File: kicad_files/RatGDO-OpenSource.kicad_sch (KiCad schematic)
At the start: 10 parts, among them J1 Screw_Terminal_01x03, J2 Screw_Terminal_01x03, Q1 2N7002, Q2 AO3400A, U1 WeMos_D1_mini, U2 AMS1117-3.3

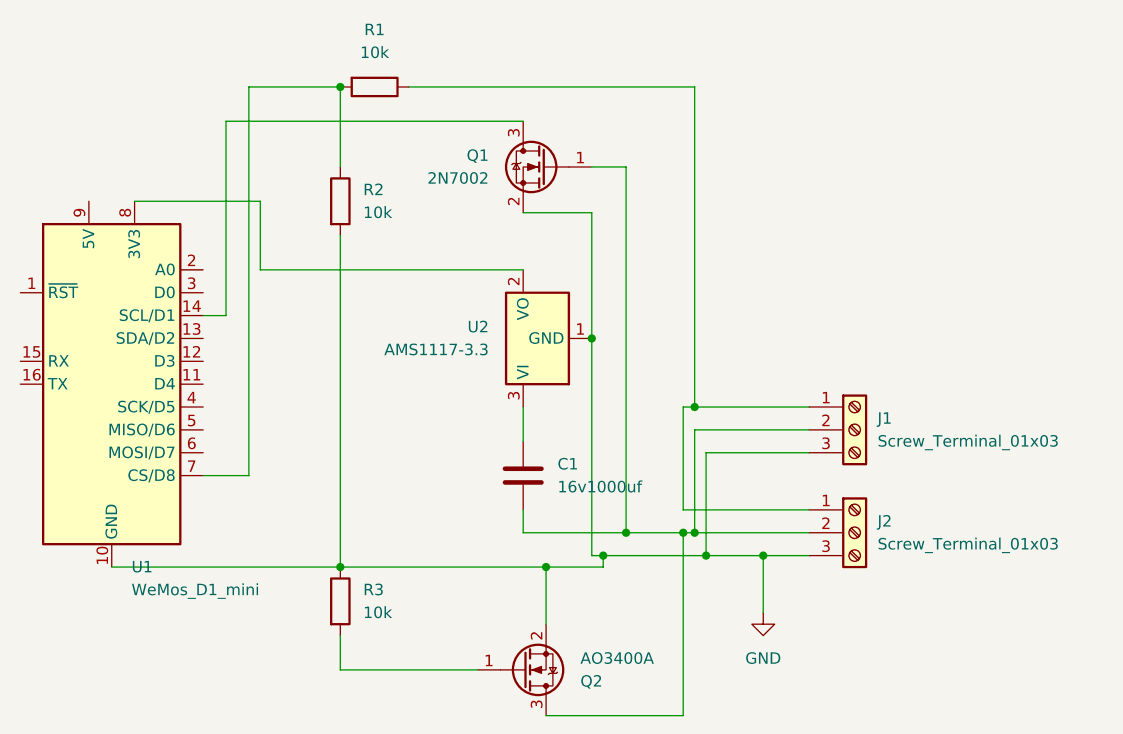
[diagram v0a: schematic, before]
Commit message: Updated Files to match new Schematics
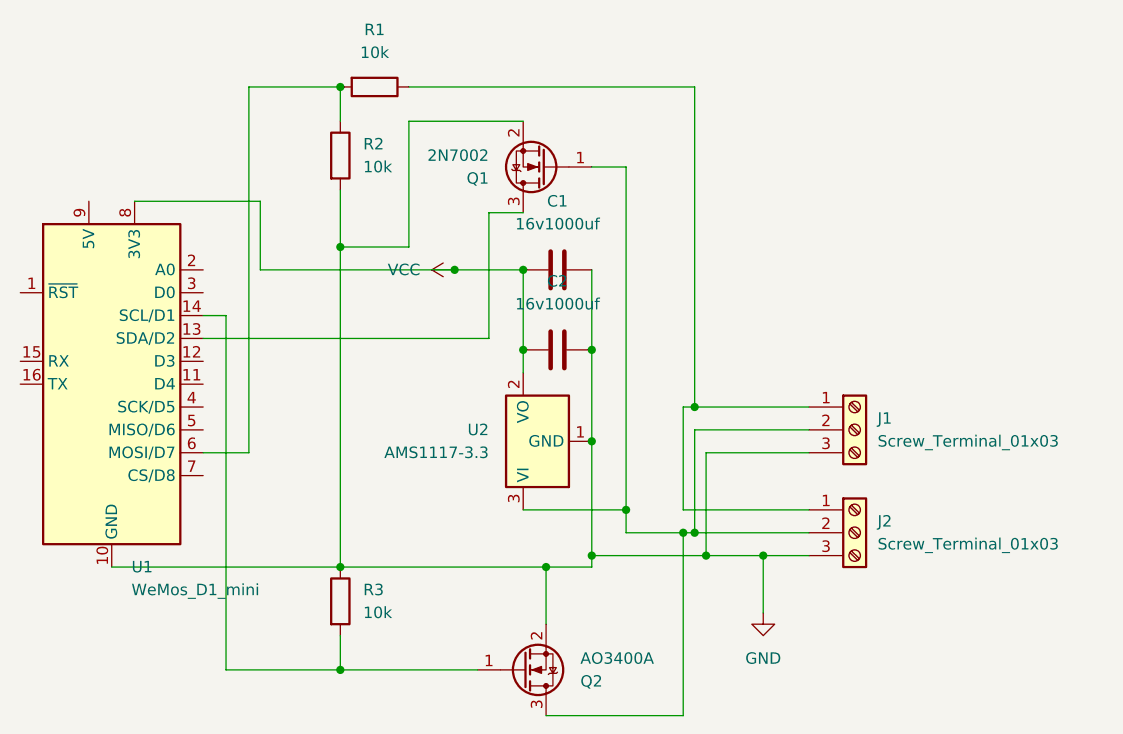
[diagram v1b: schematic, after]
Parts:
- added C2: 16v1000uf, Capacitor_THT:CP_Radial_D10.0mm_P5.00mm, symbol Device:C
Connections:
- net GND: now also C1.2, C2.2
- net at Q2.1 (G), R3.2: now also U1.14 (SCL/D1)
- net at U1.13 (SDA/D2): now also Q1.3 (D)
- net at U1.6 (MOSI/D7): now also R1.2, R2.1
- net VCC: now reaches U1.8 (3V3), U2.2 (VO)
- net VCC: now also C1.1, C2.1
- net at U2.3 (VI): now also J1.2 (Pin_2), J2.2 (Pin_2), Q1.1 (G), Q2.3 (D); no longer C1.1
- now unconnected: U1.7 (CS/D8)
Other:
- moved on the sheet: C1, Q1, R2, U2

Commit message: Remove power supply components
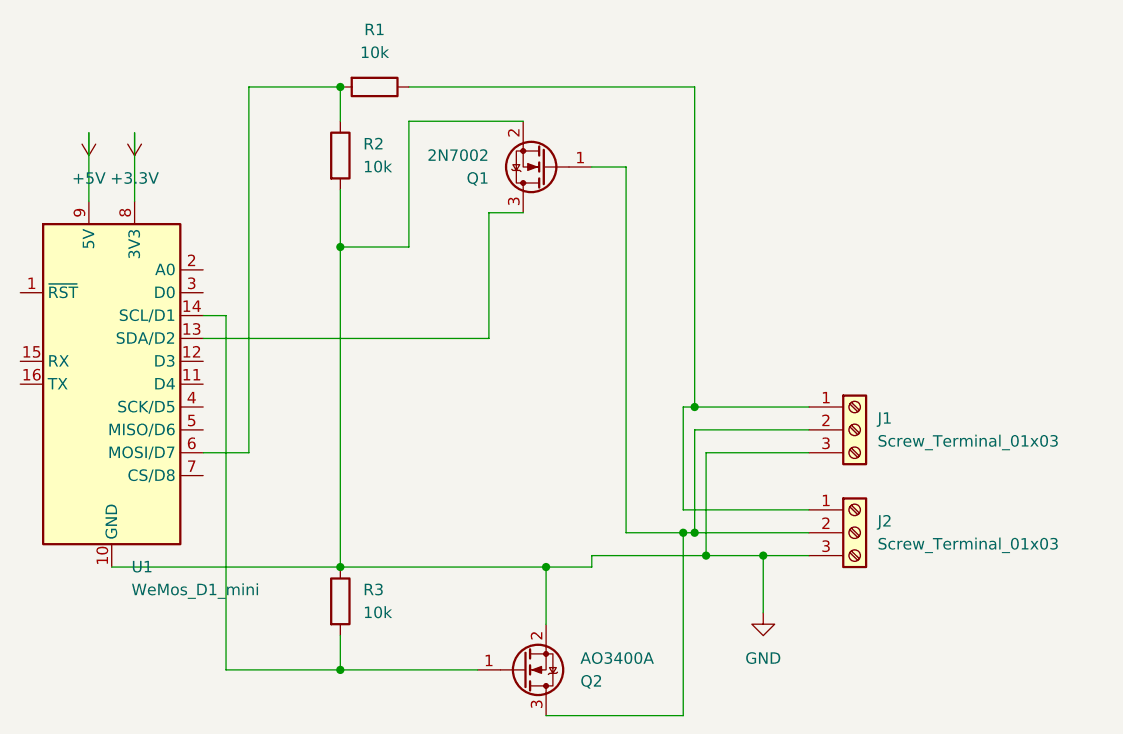
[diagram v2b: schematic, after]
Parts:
- removed C1: 16v1000uf, Capacitor_SMD:CP_Elec_10x10.5, symbol Device:C
- removed C2: 16v1000uf, Capacitor_THT:CP_Radial_D10.0mm_P5.00mm, symbol Device:C
- removed U2: AMS1117-3.3, Package_TO_SOT_SMD:SOT-223-3_TabPin2, symbol Regulator_Linear:AMS1117-3.3
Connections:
- net +5V: now reaches U1.9 (5V)
- net VCC renamed +3.3V
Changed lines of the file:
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@@
 (kicad_sch (version 20230121) (generator eeschema)
   (paper "A4")
-  (junction (at 125.73 81.28) (diameter 0) (color 0 0 0 0)
-  )
-  (junction (at 133.35 91.44) (diameter 0) (color 0 0 0 0)
-  )
-  (junction (at 125.73 72.39) (diameter 0) (color 0 0 0 0)
-  )
-  (junction (at 137.16 99.06) (diameter 0) (color 0 0 0 0)
-  )
   (junction (at 105.41 105.41) (diameter 0) (color 0 0 0 0)
   )
@@
   (junction (at 146.05 104.14) (diameter 0) (color 0 0 0 0)
   )
-  (junction (at 118.11 72.39) (diameter 0) (color 0 0 0 0)
-  )
-  (junction (at 133.35 104.14) (diameter 0) (color 0 0 0 0)
-  )
   (junction (at 152.4 104.14) (diameter 0) (color 0 0 0 0)
   )
   (junction (at 105.41 69.85) (diameter 0) (color 0 0 0 0)
   )
-  (junction (at 133.35 81.28) (diameter 0) (color 0 0 0 0)
-  )
   (junction (at 144.78 101.6) (diameter 0) (color 0 0 0 0)
   )
@@
   (junction (at 105.41 116.84) (diameter 0) (color 0 0 0 0)
   )
-  (wire (pts (xy 125.73 72.39) (xy 125.73 81.28))
-    (stroke (width 0) (type default))
-  )
-  (wire (pts (xy 96.52 72.39) (xy 118.11 72.39))
-    (stroke (width 0) (type default))
-  )
   (wire (pts (xy 128.27 121.92) (xy 143.51 121.92))
     (stroke (width 0) (type default))
@@
     (stroke (width 0) (type default))
   )
-  (wire (pts (xy 118.11 72.39) (xy 125.73 72.39))
-    (stroke (width 0) (type default))
-  )
   (wire (pts (xy 113.03 55.88) (xy 113.03 69.85))
     (stroke (width 0) (type default))
@@
     (stroke (width 0) (type default))
   )
-  (wire (pts (xy 137.16 60.96) (xy 137.16 99.06))
-    (stroke (width 0) (type default))
-  )
-  (wire (pts (xy 125.73 81.28) (xy 125.73 83.82))
+  (wire (pts (xy 137.16 60.96) (xy 137.16 101.6))
     (stroke (width 0) (type default))
   )
@@
     (stroke (width 0) (type default))
   )
-  (wire (pts (xy 133.35 72.39) (xy 133.35 81.28))
-    (stroke (width 0) (type default))
-  )
   (wire (pts (xy 128.27 105.41) (xy 128.27 111.76))
     (stroke (width 0) (type default))
@@
     (stroke (width 0) (type default))
   )
-  (wire (pts (xy 96.52 64.77) (xy 82.55 64.77))
-    (stroke (width 0) (type default))
-  )
   (wire (pts (xy 92.71 116.84) (xy 105.41 116.84))
     (stroke (width 0) (type default))
   )
-  (wire (pts (xy 133.35 91.44) (xy 133.35 104.14))
-    (stroke (width 0) (type default))
-  )
   (wire (pts (xy 90.17 80.01) (xy 121.92 80.01))
     (stroke (width 0) (type default))
@@
     (stroke (width 0) (type default))
   )
-  (wire (pts (xy 133.35 81.28) (xy 133.35 91.44))
-    (stroke (width 0) (type default))
-  )
   (wire (pts (xy 90.17 77.47) (xy 92.71 77.47))
     (stroke (width 0) (type default))
@@
     (stroke (width 0) (type default))
   )
+  (wire (pts (xy 77.47 57.15) (xy 77.47 64.77))
+    (stroke (width 0) (type default))
+  )
   (wire (pts (xy 113.03 69.85) (xy 105.41 69.85))
     (stroke (width 0) (type default))
   )
-  (wire (pts (xy 137.16 99.06) (xy 137.16 101.6))
-    (stroke (width 0) (type default))
-  )
   (wire (pts (xy 144.78 90.17) (xy 157.48 90.17))
     (stroke (width 0) (type default))
   )
+  (wire (pts (xy 82.55 57.15) (xy 82.55 64.77))
+    (stroke (width 0) (type default))
+  )
   (wire (pts (xy 105.41 116.84) (xy 105.41 113.03))
     (stroke (width 0) (type default))
@@
     (stroke (width 0) (type default))
   )
-  (wire (pts (xy 96.52 72.39) (xy 96.52 64.77))
-    (stroke (width 0) (type default))
-  )
-  (wire (pts (xy 125.73 99.06) (xy 137.16 99.06))
-    (stroke (width 0) (type default))
-  )
   (wire (pts (xy 121.92 66.04) (xy 121.92 80.01))
     (stroke (width 0) (type default))
@@
   (wire (pts (xy 105.41 52.07) (xy 105.41 55.88))
     (stroke (width 0) (type default))
+  )
+  (symbol (lib_id "power:+5V") (at 77.47 57.15 0) (mirror x) (unit 1)
+    (in_bom yes) (on_board yes) (dnp no)
+    (property "Reference" "#PWR03" (at 77.47 53.34 0)
+      (effects (font (size 1.27 1.27)) hide)
+    )
+    (property "Value" "+5V" (at 77.47 62.23 0)
+      (effects (font (size 1.27 1.27)))
+    )
+    (property "Footprint" "" (at 77.47 57.15 0)
+      (effects (font (size 1.27 1.27)) hide)
+    )
+    (property "Datasheet" "" (at 77.47 57.15 0)
+      (effects (font (size 1.27 1.27)) hide)
+    )
+    (pin "1")
+    (instances
+      (project "RatGDO-OpenSource"
+        (path "/d526daf5-1a87-4c4a-b8db-6120ccadc008"
+          (reference "#PWR03") (unit 1)
+        )
+      )
+    )
   )
   (symbol (lib_id "Device:R") (at 105.41 109.22 0) (unit 1)
@@
     )
   )
-  (symbol (lib_id "Device:C") (at 129.54 72.39 90) (unit 1)
-    (in_bom yes) (on_board yes) (dnp no) (fields_autoplaced)
-    (property "Reference" "C1" (at 129.54 64.77 90)
-      (effects (font (size 1.27 1.27)))
-    )
-    (property "Value" "16v1000uf" (at 129.54 67.31 90)
-      (effects (font (size 1.27 1.27)))
-    )
-    (property "Footprint" "Capacitor_SMD:CP_Elec_10x10.5" (at 133.35 71.4248 0)
-      (effects (font (size 1.27 1.27)) hide)
-    )
-    (property "Datasheet" "~" (at 129.54 72.39 0)
-      (effects (font (size 1.27 1.27)) hide)
-    )
-    (pin "1")
-    (pin "2")
-    (instances
-      (project "RatGDO-OpenSource"
-        (path "/d526daf5-1a87-4c4a-b8db-6120ccadc008"
-          (reference "C1") (unit 1)
-        )
-      )
-    )
-  )
   (symbol (lib_id "Connector:Screw_Terminal_01x03") (at 162.56 90.17 0) (unit 1)
     (in_bom yes) (on_board yes) (dnp no) (fields_autoplaced)
@@
         (path "/d526daf5-1a87-4c4a-b8db-6120ccadc008"
           (reference "J1") (unit 1)
-        )
-      )
-    )
-  )
-  (symbol (lib_id "power:VCC") (at 118.11 72.39 90) (unit 1)
-    (in_bom yes) (on_board yes) (dnp no) (fields_autoplaced)
-    (property "Reference" "#PWR02" (at 121.92 72.39 0)
-      (effects (font (size 1.27 1.27)) hide)
-    )
-    (property "Value" "VCC" (at 114.3 72.39 90)
-      (effects (font (size 1.27 1.27)) (justify left))
-    )
-    (property "Footprint" "" (at 118.11 72.39 0)
-      (effects (font (size 1.27 1.27)) hide)
-    )
-    (property "Datasheet" "" (at 118.11 72.39 0)
-      (effects (font (size 1.27 1.27)) hide)
-    )
-    (pin "1")
-    (instances
-      (project "RatGDO-OpenSource"
-        (path "/d526daf5-1a87-4c4a-b8db-6120ccadc008"
-          (reference "#PWR02") (unit 1)
-        )
-      )
-    )
-  )
-  (symbol (lib_id "Regulator_Linear:AMS1117-3.3") (at 125.73 91.44 90) (unit 1)
-    (in_bom yes) (on_board yes) (dnp no) (fields_autoplaced)
-    (property "Reference" "U2" (at 121.92 90.17 90)
-      (effects (font (size 1.27 1.27)) (justify left))
-    )
-    (property "Value" "AMS1117-3.3" (at 121.92 92.71 90)
-      (effects (font (size 1.27 1.27)) (justify left))
-    )
-    (property "Footprint" "Package_TO_SOT_SMD:SOT-223-3_TabPin2" (at 120.65 91.44 0)
-      (effects (font (size 1.27 1.27)) hide)
-    )
-    (property "Datasheet" "http://www.advanced-monolithic.com/pdf/ds1117.pdf" (at 132.08 88.9 0)
-      (effects (font (size 1.27 1.27)) hide)
-    )
-    (pin "1")
-    (pin "2")
-    (pin "3")
-    (instances
-      (project "RatGDO-OpenSource"
-        (path "/d526daf5-1a87-4c4a-b8db-6120ccadc008"
-          (reference "U2") (unit 1)
         )
       )
@@
         (path "/d526daf5-1a87-4c4a-b8db-6120ccadc008"
           (reference "#PWR01") (unit 1)
-        )
-      )
-    )
-  )
-  (symbol (lib_id "Device:C") (at 129.54 81.28 90) (unit 1)
-    (in_bom yes) (on_board yes) (dnp no) (fields_autoplaced)
-    (property "Reference" "C2" (at 129.54 73.66 90)
-      (effects (font (size 1.27 1.27)))
-    )
-    (property "Value" "16v1000uf" (at 129.54 76.2 90)
-      (effects (font (size 1.27 1.27)))
-    )
-    (property "Footprint" "Capacitor_THT:CP_Radial_D10.0mm_P5.00mm" (at 133.35 80.3148 0)
-      (effects (font (size 1.27 1.27)) hide)
-    )
-    (property "Datasheet" "~" (at 129.54 81.28 0)
-      (effects (font (size 1.27 1.27)) hide)
-    )
-    (pin "1")
-    (pin "2")
-    (instances
-      (project "RatGDO-OpenSource"
-        (path "/d526daf5-1a87-4c4a-b8db-6120ccadc008"
-          (reference "C2") (unit 1)
         )
       )
@@
         )
       )
+    )
+  )
+  (symbol (lib_id "power:+3.3V") (at 82.55 57.15 0) (mirror x) (unit 1)
+    (in_bom yes) (on_board yes) (dnp no)
+    (property "Reference" "#PWR02" (at 82.55 53.34 0)
+      (effects (font (size 1.27 1.27)) hide)
+    )
+    (property "Value" "+3.3V" (at 82.55 62.23 0)
+      (effects (font (size 1.27 1.27)))
+    )
+    (property "Footprint" "" (at 82.55 57.15 0)
+      (effects (font (size 1.27 1.27)) hide)
+    )
+    (property "Datasheet" "" (at 82.55 57.15 0)
+      (effects (font (size 1.27 1.27)) hide)
+    )
+    (pin "1")
+    (instances
+      (project "RatGDO-OpenSource"
+        (path "/d526daf5-1a87-4c4a-b8db-6120ccadc008"
+          (reference "#PWR02") (unit 1)
+        )
+      )
